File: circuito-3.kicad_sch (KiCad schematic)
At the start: 0 parts

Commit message: Footprints parcialmente adicionados.
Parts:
- added R10, R11, R12, R13, R14, R15, R16, R8, R9: R, symbol Device:R
- added RV2, RV3, RV4, RV5, RV6, RV7: R_Potentiometer, symbol Device:R_Potentiometer
- added U6, U7, U8: TL081, symbol Amplifier_Operational:TL081
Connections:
- new net: R10.2, RV3.3
- new net: R11.2, R12.2, R13.1, U7.2 (-)
- new net: R10.1, R8.2, R9.2, U6.2 (-)
- new net: R11.1, RV4.2
- new net: R14.1, RV6.2
- new net: R14.2, R15.2, R16.1, U8.2 (-)
- new net: R16.2, RV7.3
- new net: R13.2, RV5.3
- new net: R8.1, RV2.2
- new net +15V: RV2.1, RV4.1, RV6.1
- new net -15V: RV2.3, RV4.3, RV6.3
- new net GND: U6.3 (+), U7.3 (+), U8.3 (+)
- new net Quadrada: R9.1, RV3.1, RV3.2, U6.6
- new net Senoidal: R15.1, RV7.1, RV7.2, U8.6
- new net Triangular: R12.1, RV5.1, RV5.2, U7.6

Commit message: Relação de footprints finalizada.
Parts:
- R10, R11, R12, R13, R14, R15, R16, R8, R9: footprint (none) -> Resistor_THT:R_Axial_DIN0207_L6.3mm_D2.5mm_P2.54mm_Vertical
- RV2, RV3, RV4, RV5, RV6, RV7: footprint (none) -> Potentiometer_THT:Potentiometer_Bourns_3296W_Vertical
- U6, U7, U8: footprint (none) -> Package_DIP:DIP-8_W7.62mm_LongPads
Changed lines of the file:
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@@
 			)
 		)
-		(property "Footprint" ""
+		(property "Footprint" "Potentiometer_THT:Potentiometer_Bourns_3296W_Vertical"
 			(at 83.82 92.71 0)
 			(effects
@@
 			)
 		)
-		(property "Footprint" ""
+		(property "Footprint" "Package_DIP:DIP-8_W7.62mm_LongPads"
 			(at 166.37 72.39 0)
 			(effects
@@
 			)
 		)
-		(property "Footprint" ""
+		(property "Footprint" "Resistor_THT:R_Axial_DIN0207_L6.3mm_D2.5mm_P2.54mm_Vertical"
 			(at 52.07 79.248 90)
 			(effects
@@
 			)
 		)
-		(property "Footprint" ""
+		(property "Footprint" "Package_DIP:DIP-8_W7.62mm_LongPads"
 			(at 76.2 73.66 0)
 			(effects
@@
 			)
 		)
-		(property "Footprint" ""
+		(property "Footprint" "Potentiometer_THT:Potentiometer_Bourns_3296W_Vertical"
 			(at 127 93.98 0)
 			(effects
@@
 			)
 		)
-		(property "Footprint" ""
+		(property "Footprint" "Potentiometer_THT:Potentiometer_Bourns_3296W_Vertical"
 			(at 210.82 92.71 0)
 			(effects
@@
 			)
 		)
-		(property "Footprint" ""
+		(property "Footprint" "Resistor_THT:R_Axial_DIN0207_L6.3mm_D2.5mm_P2.54mm_Vertical"
 			(at 224.79 94.488 90)
 			(effects
@@
 			)
 		)
-		(property "Footprint" ""
+		(property "Footprint" "Resistor_THT:R_Axial_DIN0207_L6.3mm_D2.5mm_P2.54mm_Vertical"
 			(at 71.12 94.488 90)
 			(effects
@@
 			)
 		)
-		(property "Footprint" ""
+		(property "Footprint" "Resistor_THT:R_Axial_DIN0207_L6.3mm_D2.5mm_P2.54mm_Vertical"
 			(at 226.06 76.708 90)
 			(effects
@@
 			)
 		)
-		(property "Footprint" ""
+		(property "Footprint" "Resistor_THT:R_Axial_DIN0207_L6.3mm_D2.5mm_P2.54mm_Vertical"
 			(at 140.97 95.758 90)
 			(effects
@@
 			)
 		)
-		(property "Footprint" ""
+		(property "Footprint" "Potentiometer_THT:Potentiometer_Bourns_3296W_Vertical"
 			(at 257.81 90.17 0)
 			(effects
@@
 			)
 		)
-		(property "Footprint" ""
+		(property "Footprint" "Resistor_THT:R_Axial_DIN0207_L6.3mm_D2.5mm_P2.54mm_Vertical"
 			(at 245.11 91.948 90)
 			(effects
@@
 			)
 		)
-		(property "Footprint" ""
+		(property "Footprint" "Potentiometer_THT:Potentiometer_Bourns_3296W_Vertical"
 			(at 173.99 91.44 0)
 			(effects
@@
 			)
 		)
-		(property "Footprint" ""
+		(property "Footprint" "Resistor_THT:R_Axial_DIN0207_L6.3mm_D2.5mm_P2.54mm_Vertical"
 			(at 161.29 93.218 90)
 			(effects
@@
 			)
 		)
-		(property "Footprint" ""
+		(property "Footprint" "Resistor_THT:R_Axial_DIN0207_L6.3mm_D2.5mm_P2.54mm_Vertical"
 			(at 142.24 77.978 90)
 			(effects
@@
 			)
 		)
-		(property "Footprint" ""
+		(property "Footprint" "Package_DIP:DIP-8_W7.62mm_LongPads"
 			(at 250.19 71.12 0)
 			(effects
@@
 			)
 		)
-		(property "Footprint" ""
+		(property "Footprint" "Potentiometer_THT:Potentiometer_Bourns_3296W_Vertical"
 			(at 36.83 95.25 0)
 			(effects
@@
 			)
 		)
-		(property "Footprint" ""
+		(property "Footprint" "Resistor_THT:R_Axial_DIN0207_L6.3mm_D2.5mm_P2.54mm_Vertical"
 			(at 50.8 97.028 90)
 			(effects

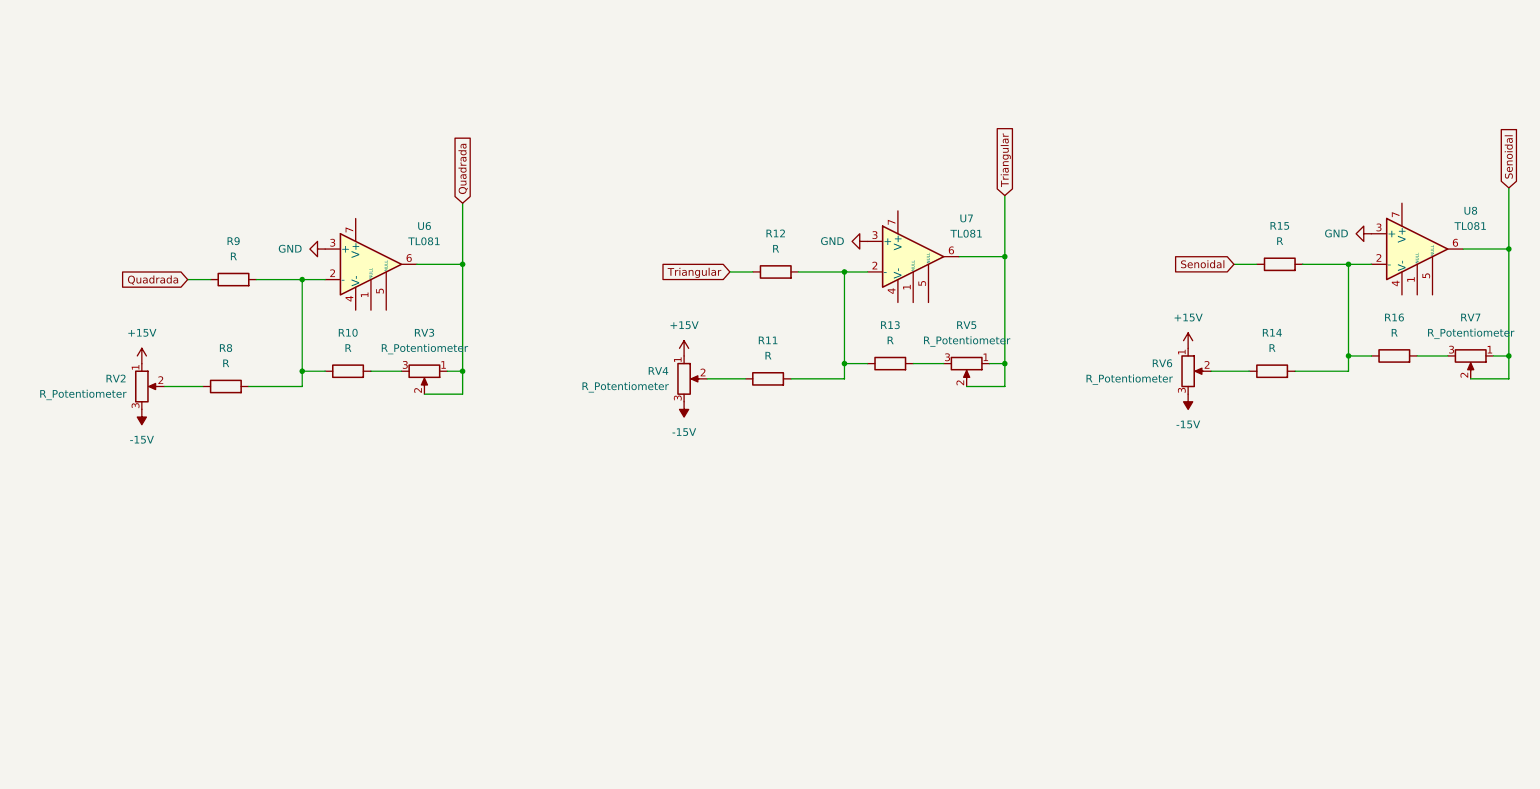
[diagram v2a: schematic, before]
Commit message: Alterações no schematic para bater com o que o professor mandoou no gropo. Pendente revisão.
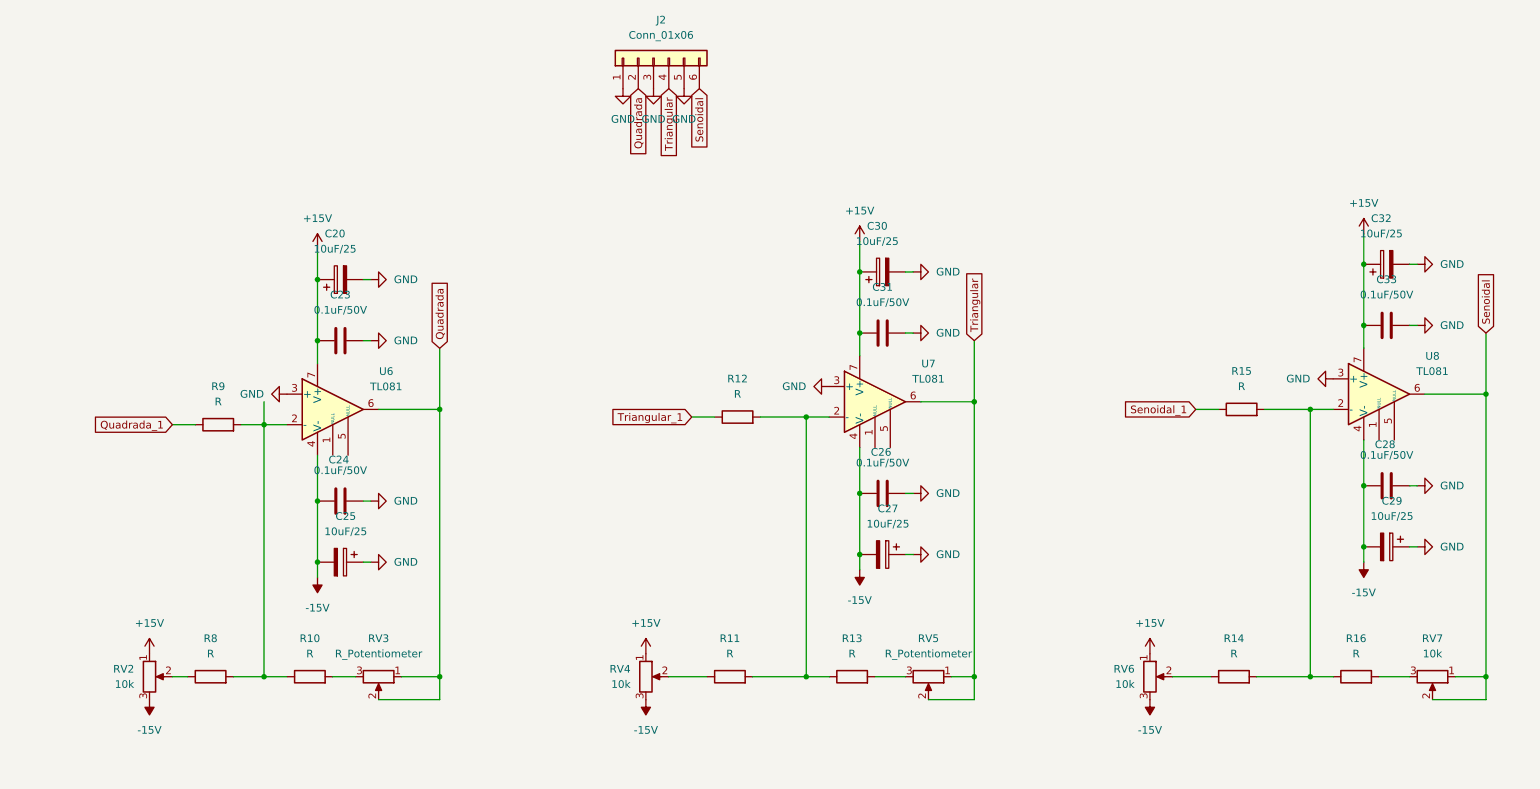
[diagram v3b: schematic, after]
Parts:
- added C20, C25, C27, C29, C30, C32: 10uF/25, Capacitor_THT:CP_Radial_D4.0mm_P2.00mm, symbol Device:C_Polarized
- added C23, C24, C26, C28, C31, C33: 0.1uF/50V, Capacitor_THT:C_Disc_D3.8mm_W2.6mm_P2.50mm, symbol Device:C
- added J2: Conn_01x06, Connector_PinHeader_2.54mm:PinHeader_1x06_P2.54mm_Vertical, symbol Connector_Generic:Conn_01x06
- RV2, RV4, RV6, RV7: value R_Potentiometer -> 10k
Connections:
- net +15V: now also U6.7 (V+), U7.7 (V+), U8.7 (V+), C20.1, C23.1, C30.1, C31.1, C32.1, C33.1
- net -15V: now also U6.4 (V-), U7.4 (V-), U8.4 (V-), C24.1, C25.2, C26.1, C27.2, C28.1, C29.2
- net GND: now also C20.2, C23.2, C24.2, C25.1, C26.2, C27.1, C28.2, C29.1, C30.2, C31.2, C32.2, C33.2, J2.1 (Pin_1), J2.3 (Pin_3), J2.5 (Pin_5)
- net Quadrada: now also J2.2 (Pin_2); no longer R9.1
- net Senoidal: now also J2.6 (Pin_6); no longer R15.1
- net Triangular: now also J2.4 (Pin_4); no longer R12.1
- new net Quadrada_1: R9.1
- new net Senoidal_1: R15.1
- new net Triangular_1: R12.1
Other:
- moved on the sheet: R10, R11, R12, R13, R14, R15, R16, R8, R9, RV2, RV3, RV4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

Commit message: Revisão de schematics finalizado. Posicionamentos dos componentes do circuito 1 e 2 no PCB editor.
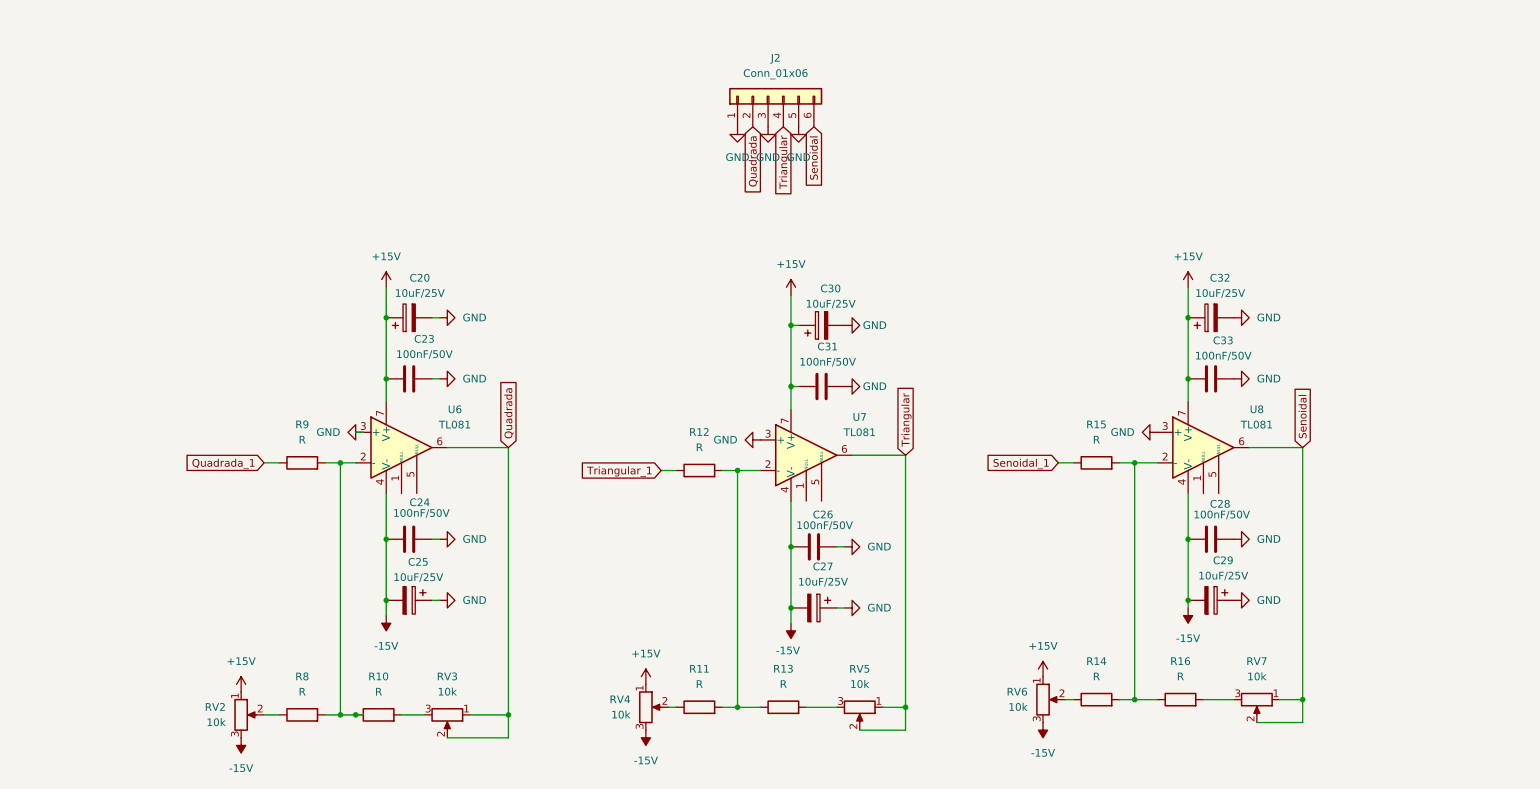
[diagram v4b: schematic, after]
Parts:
- C20, C25, C27, C29, C30, C32: value 10uF/25 -> 10uF/25V; footprint Capacitor_THT:CP_Radial_D4.0mm_P2.00mm -> Capacitor_SMD:CP_Elec_4x5.8
- C23, C24, C26, C28, C31, C33: value 0.1uF/50V -> 100nF/50V; footprint Capacitor_THT:C_Disc_D3.8mm_W2.6mm_P2.50mm -> Capacitor_SMD:C_0805_2012Metric
- R10, R11, R12, R13, R14, R15, R16, R8, R9: footprint Resistor_THT:R_Axial_DIN0207_L6.3mm_D2.5mm_P2.54mm_Vertical -> Resistor_SMD:R_0805_2012Metric
- RV3, RV5: value R_Potentiometer -> 10k
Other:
- moved on the sheet: C20, C23, C24, C25, C26, C27, C28, C29, C30, C31, C32, C33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
